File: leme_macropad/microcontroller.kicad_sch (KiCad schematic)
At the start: 23 parts, among them U1 W25Q128JVS, U2 RP2040, Y1 ABM8-272-T3

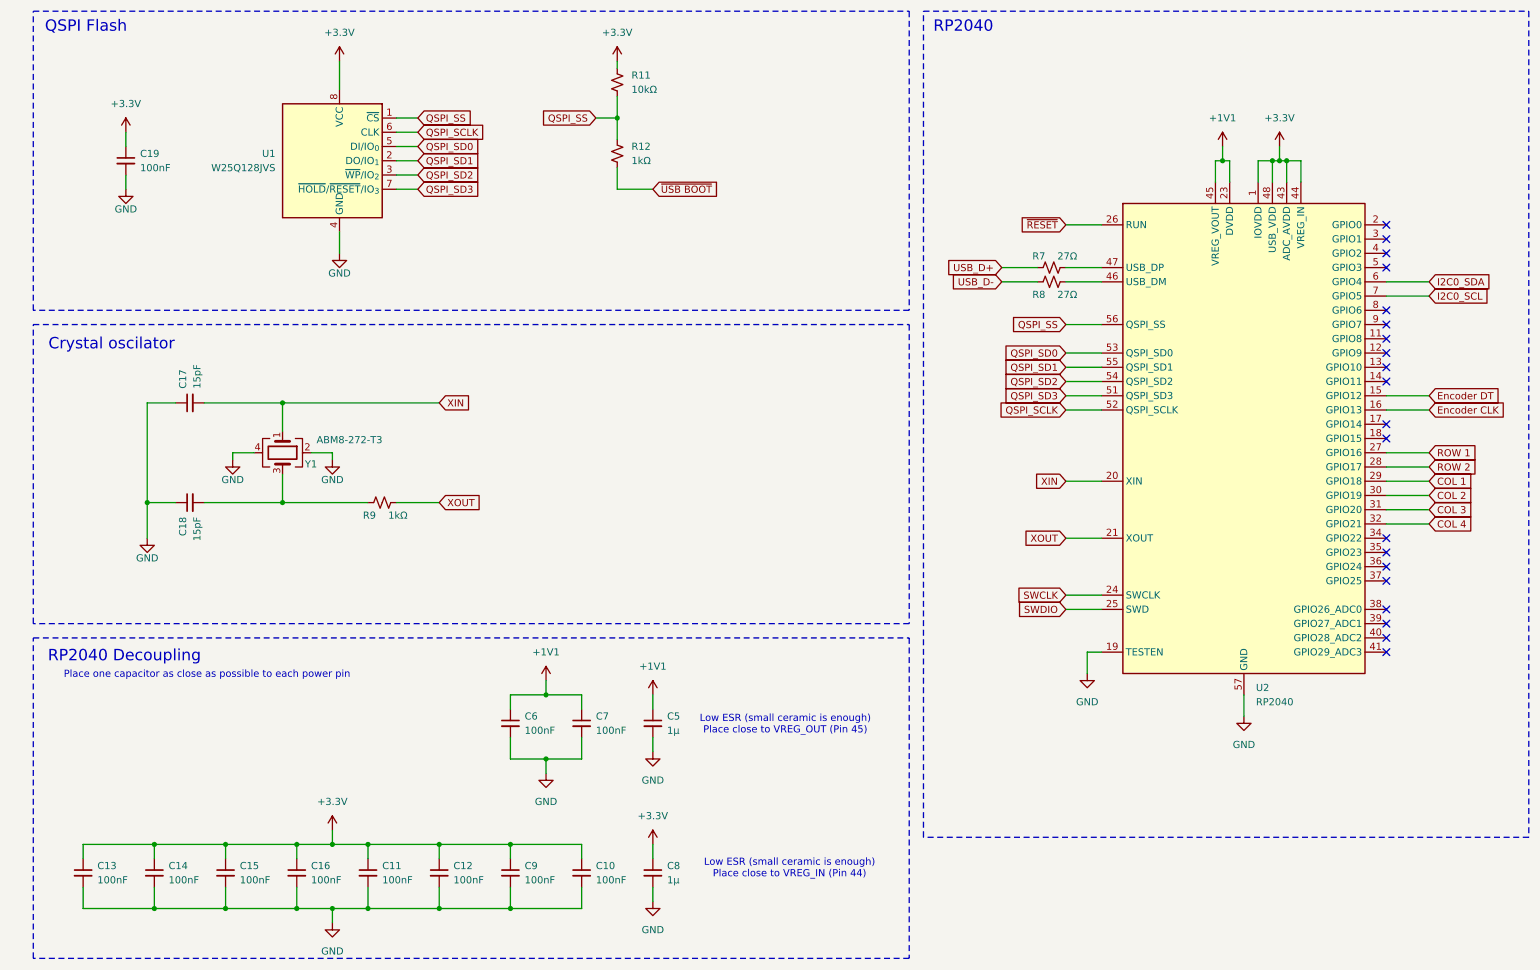
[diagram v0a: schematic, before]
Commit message: Annotates schematics again
Everything changed a lot, so it makes sense to reorder the components.
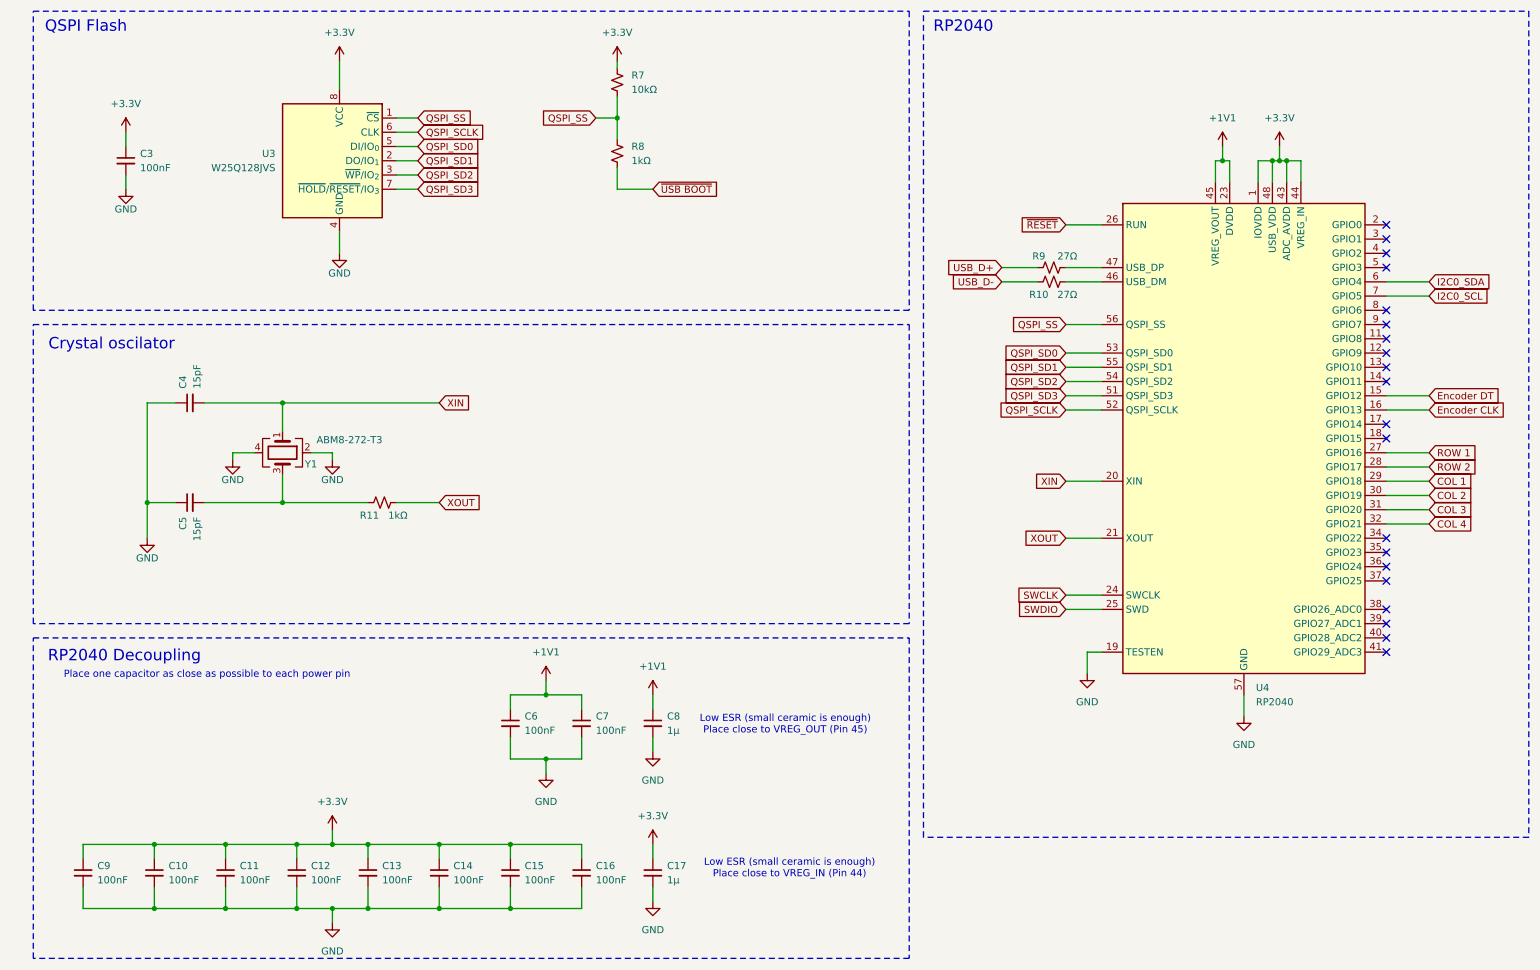
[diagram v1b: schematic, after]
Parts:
- renumbered C14 to C10, C15 to C11, C16 to C12, C11 to C13, C12 to C14, C9 to C15, C10 to C16, C8 to C17, C19 to C3, C17 to C4, C18 to C5, C5 to C8, C13 to C9, R8 to R10, R9 to R11, R11 to R7, R12 to R8, R7 to R9, U1 to U3, U2 to U4

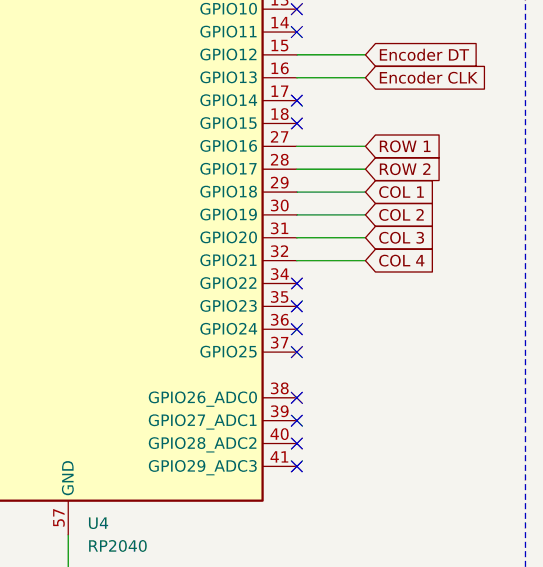
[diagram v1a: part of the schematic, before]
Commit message: Adds RGB LED matrix
There's only one per switch for now.
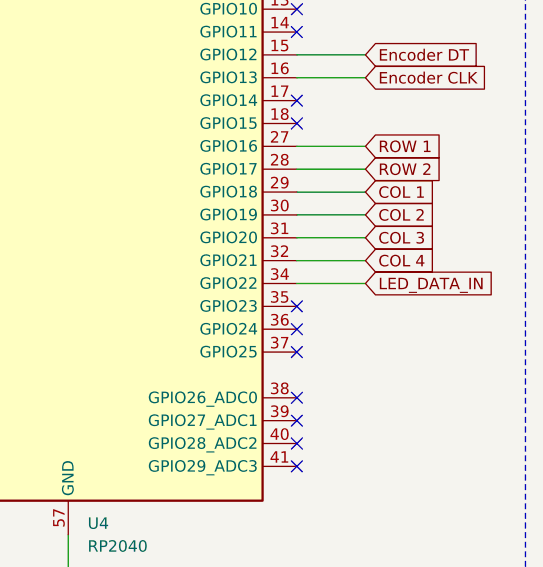
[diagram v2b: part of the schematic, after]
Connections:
- net LED_DATA_IN: now reaches U4.34 (GPIO22)
- no-connect marks 20 -> 19
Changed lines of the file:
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@@
-	)
-	(no_connect
-		(at 256.54 109.22)
 	)
 	(no_connect
@@
 	(wire
 		(pts
+			(xy 256.54 109.22) (xy 264.16 109.22)
+		)
+		(stroke
+			(width 0)
+			(type default)
+		)
+	)
+	(wire
+		(pts
 			(xy 59.69 85.09) (xy 45.72 85.09)
 		)
@@
 			(effects
 				(font
+					(size 1.27 1.27)
+				)
+				(justify left)
+				(hide yes)
+			)
+		)
+	)
+	(global_label "LED_DATA_IN"
+		(shape input)
+		(at 264.16 109.22 0)
+		(fields_autoplaced yes)
+		(effects
+			(font
+				(size 1.27 1.27)
+			)
+			(justify left)
+		)
+		(property "Intersheetrefs" "${INTERSHEET_REFS}"
+			(at 278.8776 109.22 0)
+			(effects
+				(font

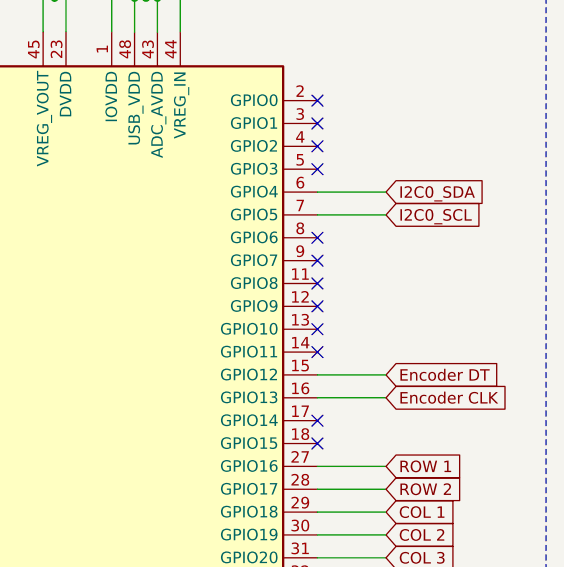
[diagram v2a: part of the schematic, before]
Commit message: Adds testpoints to some free GPIOs
It doesn't hurt to have them broken out if we need it.
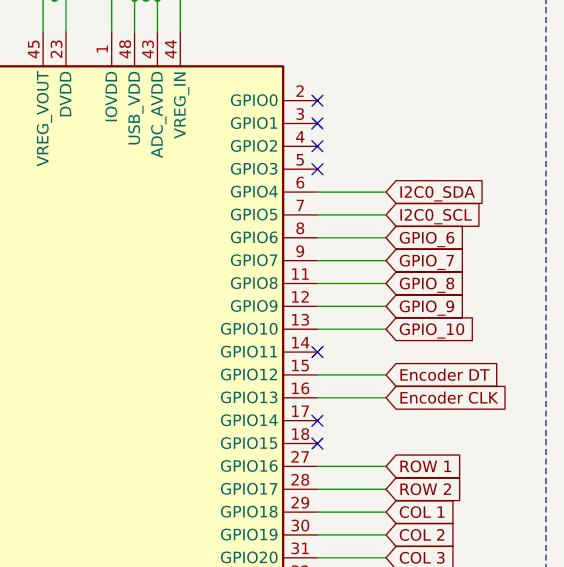
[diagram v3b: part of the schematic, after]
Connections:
- net GPIO_8: now reaches U4.11 (GPIO8)
- net GPIO_9: now reaches U4.12 (GPIO9)
- net GPIO_10: now reaches U4.13 (GPIO10)
- net GPIO_6: now reaches U4.8 (GPIO6)
- net GPIO_7: now reaches U4.9 (GPIO7)
- no-connect marks 19 -> 14
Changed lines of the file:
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@@
-	)
-	(no_connect
-		(at 256.54 73.66)
 	)
 	(no_connect
@@
 	)
 	(no_connect
-		(at 256.54 71.12)
+		(at 256.54 81.28)
 	)
 	(no_connect
@@
 	)
 	(no_connect
-		(at 256.54 81.28)
-	)
-	(no_connect
 		(at 256.54 91.44)
 	)
@@
 	)
 	(no_connect
-		(at 256.54 68.58)
-	)
-	(no_connect
-		(at 256.54 78.74)
-	)
-	(no_connect
 		(at 256.54 55.88)
 	)
@@
 		(at 256.54 60.96)
 	)
-	(no_connect
-		(at 256.54 76.2)
-	)
 	(wire
 		(pts
@@
 	(wire
 		(pts
+			(xy 256.54 73.66) (xy 264.16 73.66)
+		)
+		(stroke
+			(width 0)
+			(type default)
+		)
+	)
+	(wire
+		(pts
 			(xy 226.06 45.72) (xy 226.06 41.91)
 		)
@@
 	(wire
 		(pts
+			(xy 256.54 71.12) (xy 264.16 71.12)
+		)
+		(stroke
+			(width 0)
+			(type default)
+		)
+	)
+	(wire
+		(pts
 			(xy 199.39 63.5) (xy 205.74 63.5)
 		)
@@
 	(wire
 		(pts
+			(xy 256.54 68.58) (xy 264.16 68.58)
+		)
+		(stroke
+			(width 0)
+			(type default)
+		)
+	)
+	(wire
+		(pts
 			(xy 199.39 109.22) (xy 205.74 109.22)
 		)
@@
 	(wire
 		(pts
+			(xy 256.54 76.2) (xy 264.16 76.2)
+		)
+		(stroke
+			(width 0)
+			(type default)
+		)
+	)
+	(wire
+		(pts
 			(xy 106.68 137.16) (xy 113.03 137.16)
 		)
@@
 	(wire
 		(pts
+			(xy 256.54 78.74) (xy 264.16 78.74)
+		)
+		(stroke
+			(width 0)
+			(type default)
+		)
+	)
+	(wire
+		(pts
 			(xy 24.13 171.45) (xy 24.13 175.26)
 		)
@@
 		)
 	)
+	(global_label "GPIO_7"
+		(shape input)
+		(at 264.16 71.12 0)
+		(fields_autoplaced yes)
+		(effects
+			(font
+				(size 1.27 1.27)
+			)
+			(justify left)
+		)
+		(property "Intersheetrefs" "${INTERSHEET_REFS}"
+			(at 273.7976 71.12 0)
+			(effects
+				(font
+					(size 1.27 1.27)
+				)
+				(justify left)
+				(hide yes)
+			)
+		)
+	)
 	(global_label "COL 4"
 		(shape input)
@@
 		)
 	)
+	(global_label "GPIO_8"
+		(shape input)
+		(at 264.16 73.66 0)
+		(fields_autoplaced yes)
+		(effects
+			(font
+				(size 1.27 1.27)
+			)
+			(justify left)
+		)
+		(property "Intersheetrefs" "${INTERSHEET_REFS}"
+			(at 273.7976 73.66 0)
+			(effects
+				(font
+					(size 1.27 1.27)
+				)
+				(justify left)
+				(hide yes)
+			)
+		)
+	)
 	(global_label "ROW 2"
 		(shape input)
@@
 		)
 	)
+	(global_label "GPIO_10"
+		(shape input)
+		(at 264.16 78.74 0)
+		(fields_autoplaced yes)
+		(effects
+			(font
+				(size 1.27 1.27)
+			)
+			(justify left)
+		)
+		(property "Intersheetrefs" "${INTERSHEET_REFS}"
+			(at 275.0071 78.74 0)
+			(effects
+				(font
+					(size 1.27 1.27)
+				)
+				(justify left)
+				(hide yes)
+			)
+		)
+	)
 	(global_label "XIN"
 		(shape input)
@@
 		)
 	)
+	(global_label "GPIO_9"
+		(shape input)
+		(at 264.16 76.2 0)
+		(fields_autoplaced yes)
+		(effects
+			(font
+				(size 1.27 1.27)
+			)
+			(justify left)
+		)
+		(property "Intersheetrefs" "${INTERSHEET_REFS}"
+			(at 273.7976 76.2 0)
+			(effects
+				(font
+					(size 1.27 1.27)
+				)
+				(justify left)
+				(hide yes)
+			)
+		)
+	)
 	(global_label "I2C0_SDA"
 		(shape input)
@@
 				(hide yes)
 			)
+		)
+	)
+	(global_label "GPIO_6"
+		(shape input)
+		(at 264.16 68.58 0)
+		(fields_autoplaced yes)
+		(effects
+			(font
+				(size 1.27 1.27)
+			)
+			(justify left)
+		)
+		(property "Intersheetrefs" "${INTERSHEET_REFS}"
+			(at 273.7976 68.58 0)
+			(effects
+				(font
+					(size 1.27 1.27)
+				)
+				(justify left)
+				(hide yes)
+			)

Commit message: Re-annotates schematics
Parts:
- renumbered C13 to C10, C14 to C11, C6 to C12, C15 to C13, C7 to C14, C16 to C15, C8 to C16, C9 to C3, C3 to C4, C10 to C5, C4 to C6, C5 to C7, C11 to C8, C12 to C9, R11 to R3, R7 to R4, R8 to R5, R9 to R6, R10 to R7

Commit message: Assigns footprints to all components in schematics
Passives are 0603, but if the layout gets too dificult (specially around
the RP2040) we might want to decrease the size.

The mechanical switches are set as hotswap sockets for Kailh v1/v2, but
after routing everything we might want to do a version for MX switches.
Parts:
- C10, C11, C12, C13, C14, C15, C16, C17, C3, C4, C5, C6, C7, C8, C9: footprint (none) -> Capacitor_SMD:C_0603_1608Metric_Pad1.08x0.95mm_HandSolder
- R3, R4, R5, R6, R7: footprint (none) -> Resistor_SMD:R_0603_1608Metric_Pad0.98x0.95mm_HandSolder
- Y1: footprint (none) -> Crystal:Crystal_SMD_3225-4Pin_3.2x2.5mm
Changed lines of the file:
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@@
 			)
 		)
-		(property "Footprint" ""
+		(property "Footprint" "Capacitor_SMD:C_0603_1608Metric_Pad1.08x0.95mm_HandSolder"
 			(at 31.75 41.91 0)
 			(effects
@@
 			)
 		)
-		(property "Footprint" ""
+		(property "Footprint" "Resistor_SMD:R_0603_1608Metric_Pad0.98x0.95mm_HandSolder"
 			(at 119.38 40.64 0)
 			(effects
@@
 			)
 		)
-		(property "Footprint" ""
+		(property "Footprint" "Resistor_SMD:R_0603_1608Metric_Pad0.98x0.95mm_HandSolder"
 			(at 196.85 60.96 0)
 			(effects
@@
 			)
 		)
-		(property "Footprint" ""
+		(property "Footprint" "Capacitor_SMD:C_0603_1608Metric_Pad1.08x0.95mm_HandSolder"
 			(at 43.18 85.09 0)
 			(effects
@@
 			)
 		)
-		(property "Footprint" ""
+		(property "Footprint" "Capacitor_SMD:C_0603_1608Metric_Pad1.08x0.95mm_HandSolder"
 			(at 100.33 142.24 0)
 			(effects
@@
 			)
 		)
-		(property "Footprint" ""
+		(property "Footprint" "Capacitor_SMD:C_0603_1608Metric_Pad1.08x0.95mm_HandSolder"
 			(at 49.53 168.91 0)
 			(effects
@@
 			)
 		)
-		(property "Footprint" ""
+		(property "Footprint" "Resistor_SMD:R_0603_1608Metric_Pad0.98x0.95mm_HandSolder"
 			(at 196.85 63.5 0)
 			(effects
@@
 			)
 		)
-		(property "Footprint" ""
+		(property "Footprint" "Capacitor_SMD:C_0603_1608Metric_Pad1.08x0.95mm_HandSolder"
 			(at 62.23 168.91 0)
 			(effects
@@
 			)
 		)
-		(property "Footprint" ""
+		(property "Footprint" "Capacitor_SMD:C_0603_1608Metric_Pad1.08x0.95mm_HandSolder"
 			(at 43.18 102.87 0)
 			(effects
@@
 			)
 		)
-		(property "Footprint" ""
+		(property "Footprint" "Capacitor_SMD:C_0603_1608Metric_Pad1.08x0.95mm_HandSolder"
 			(at 125.73 142.24 0)
 			(effects
@@
 			)
 		)
-		(property "Footprint" ""
+		(property "Footprint" "Capacitor_SMD:C_0603_1608Metric_Pad1.08x0.95mm_HandSolder"
 			(at 113.03 168.91 0)
 			(effects
@@
 			)
 		)
-		(property "Footprint" ""
+		(property "Footprint" "Capacitor_SMD:C_0603_1608Metric_Pad1.08x0.95mm_HandSolder"
 			(at 24.13 168.91 0)
 			(effects
@@
 			)
 		)
-		(property "Footprint" ""
+		(property "Footprint" "Capacitor_SMD:C_0603_1608Metric_Pad1.08x0.95mm_HandSolder"
 			(at 125.73 168.91 0)
 			(effects
@@
 			)
 		)
-		(property "Footprint" ""
+		(property "Footprint" "Resistor_SMD:R_0603_1608Metric_Pad0.98x0.95mm_HandSolder"
 			(at 119.38 27.94 0)
 			(effects
@@
 			)
 		)
-		(property "Footprint" ""
+		(property "Footprint" "Resistor_SMD:R_0603_1608Metric_Pad0.98x0.95mm_HandSolder"
 			(at 77.47 102.87 0)
 			(effects
@@
 			)
 		)
-		(property "Footprint" ""
+		(property "Footprint" "Capacitor_SMD:C_0603_1608Metric_Pad1.08x0.95mm_HandSolder"
 			(at 87.63 168.91 0)
 			(effects
@@
 			)
 		)
-		(property "Footprint" ""
+		(property "Footprint" "Crystal:Crystal_SMD_3225-4Pin_3.2x2.5mm"
 			(at 59.69 93.98 0)
 			(effects
@@
 			)
 		)
-		(property "Footprint" ""
+		(property "Footprint" "Capacitor_SMD:C_0603_1608Metric_Pad1.08x0.95mm_HandSolder"
 			(at 74.93 168.91 0)
 			(effects
@@
 			)
 		)
-		(property "Footprint" ""
+		(property "Footprint" "Capacitor_SMD:C_0603_1608Metric_Pad1.08x0.95mm_HandSolder"
 			(at 113.03 142.24 0)
 			(effects
@@
 			)
 		)
-		(property "Footprint" ""
+		(property "Footprint" "Capacitor_SMD:C_0603_1608Metric_Pad1.08x0.95mm_HandSolder"
 			(at 100.33 168.91 0)
 			(effects
@@
 			)
 		)
-		(property "Footprint" ""
+		(property "Footprint" "Capacitor_SMD:C_0603_1608Metric_Pad1.08x0.95mm_HandSolder"
 			(at 36.83 168.91 0)
 			(effects

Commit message: Changes resistors and capacitors to 0402
This should make it much easier to route things and to comply with the
signal integrity needs of some parts of the circuit.
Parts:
- C10, C11, C12, C13, C14, C15, C16, C17, C3, C4, C5, C6, C7, C8, C9: footprint Capacitor_SMD:C_0603_1608Metric_Pad1.08x0.95mm_HandSolder -> Capacitor_SMD:C_0402_1005Metric_Pad0.74x0.62mm_HandSolder
- R3, R4, R5, R6, R7: footprint Resistor_SMD:R_0603_1608Metric_Pad0.98x0.95mm_HandSolder -> Resistor_SMD:R_0402_1005Metric_Pad0.72x0.64mm_HandSolder
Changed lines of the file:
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@@
 			)
 		)
-		(property "Footprint" "Capacitor_SMD:C_0603_1608Metric_Pad1.08x0.95mm_HandSolder"
+		(property "Footprint" "Capacitor_SMD:C_0402_1005Metric_Pad0.74x0.62mm_HandSolder"
 			(at 31.75 41.91 0)
 			(effects
@@
 			)
 		)
-		(property "Footprint" "Resistor_SMD:R_0603_1608Metric_Pad0.98x0.95mm_HandSolder"
+		(property "Footprint" "Resistor_SMD:R_0402_1005Metric_Pad0.72x0.64mm_HandSolder"
 			(at 119.38 40.64 0)
 			(effects
@@
 			)
 		)
-		(property "Footprint" "Resistor_SMD:R_0603_1608Metric_Pad0.98x0.95mm_HandSolder"
+		(property "Footprint" "Resistor_SMD:R_0402_1005Metric_Pad0.72x0.64mm_HandSolder"
 			(at 196.85 60.96 0)
 			(effects
@@
 			)
 		)
-		(property "Footprint" "Capacitor_SMD:C_0603_1608Metric_Pad1.08x0.95mm_HandSolder"
+		(property "Footprint" "Capacitor_SMD:C_0402_1005Metric_Pad0.74x0.62mm_HandSolder"
 			(at 43.18 85.09 0)
 			(effects
@@
 			)
 		)
-		(property "Footprint" "Capacitor_SMD:C_0603_1608Metric_Pad1.08x0.95mm_HandSolder"
+		(property "Footprint" "Capacitor_SMD:C_0402_1005Metric_Pad0.74x0.62mm_HandSolder"
 			(at 100.33 142.24 0)
 			(effects
@@
 			)
 		)
-		(property "Footprint" "Capacitor_SMD:C_0603_1608Metric_Pad1.08x0.95mm_HandSolder"
+		(property "Footprint" "Capacitor_SMD:C_0402_1005Metric_Pad0.74x0.62mm_HandSolder"
 			(at 49.53 168.91 0)
 			(effects
@@
 			)
 		)
-		(property "Footprint" "Resistor_SMD:R_0603_1608Metric_Pad0.98x0.95mm_HandSolder"
+		(property "Footprint" "Resistor_SMD:R_0402_1005Metric_Pad0.72x0.64mm_HandSolder"
 			(at 196.85 63.5 0)
 			(effects
@@
 			)
 		)
-		(property "Footprint" "Capacitor_SMD:C_0603_1608Metric_Pad1.08x0.95mm_HandSolder"
+		(property "Footprint" "Capacitor_SMD:C_0402_1005Metric_Pad0.74x0.62mm_HandSolder"
 			(at 62.23 168.91 0)
 			(effects
@@
 			)
 		)
-		(property "Footprint" "Capacitor_SMD:C_0603_1608Metric_Pad1.08x0.95mm_HandSolder"
+		(property "Footprint" "Capacitor_SMD:C_0402_1005Metric_Pad0.74x0.62mm_HandSolder"
 			(at 43.18 102.87 0)
 			(effects
@@
 			)
 		)
-		(property "Footprint" "Capacitor_SMD:C_0603_1608Metric_Pad1.08x0.95mm_HandSolder"
+		(property "Footprint" "Capacitor_SMD:C_0402_1005Metric_Pad0.74x0.62mm_HandSolder"
 			(at 125.73 142.24 0)
 			(effects
@@
 			)
 		)
-		(property "Footprint" "Capacitor_SMD:C_0603_1608Metric_Pad1.08x0.95mm_HandSolder"
+		(property "Footprint" "Capacitor_SMD:C_0402_1005Metric_Pad0.74x0.62mm_HandSolder"
 			(at 113.03 168.91 0)
 			(effects
@@
 			)
 		)
-		(property "Footprint" "Capacitor_SMD:C_0603_1608Metric_Pad1.08x0.95mm_HandSolder"
+		(property "Footprint" "Capacitor_SMD:C_0402_1005Metric_Pad0.74x0.62mm_HandSolder"
 			(at 24.13 168.91 0)
 			(effects
@@
 			)
 		)
-		(property "Footprint" "Capacitor_SMD:C_0603_1608Metric_Pad1.08x0.95mm_HandSolder"
+		(property "Footprint" "Capacitor_SMD:C_0402_1005Metric_Pad0.74x0.62mm_HandSolder"
 			(at 125.73 168.91 0)
 			(effects
@@
 			)
 		)
-		(property "Footprint" "Resistor_SMD:R_0603_1608Metric_Pad0.98x0.95mm_HandSolder"
+		(property "Footprint" "Resistor_SMD:R_0402_1005Metric_Pad0.72x0.64mm_HandSolder"
 			(at 119.38 27.94 0)
 			(effects
@@
 			)
 		)
-		(property "Footprint" "Resistor_SMD:R_0603_1608Metric_Pad0.98x0.95mm_HandSolder"
+		(property "Footprint" "Resistor_SMD:R_0402_1005Metric_Pad0.72x0.64mm_HandSolder"
 			(at 77.47 102.87 0)
 			(effects
@@
 			)
 		)
-		(property "Footprint" "Capacitor_SMD:C_0603_1608Metric_Pad1.08x0.95mm_HandSolder"
+		(property "Footprint" "Capacitor_SMD:C_0402_1005Metric_Pad0.74x0.62mm_HandSolder"
 			(at 87.63 168.91 0)
 			(effects
@@
 			)
 		)
-		(property "Footprint" "Capacitor_SMD:C_0603_1608Metric_Pad1.08x0.95mm_HandSolder"
+		(property "Footprint" "Capacitor_SMD:C_0402_1005Metric_Pad0.74x0.62mm_HandSolder"
 			(at 74.93 168.91 0)
 			(effects
@@
 			)
 		)
-		(property "Footprint" "Capacitor_SMD:C_0603_1608Metric_Pad1.08x0.95mm_HandSolder"
+		(property "Footprint" "Capacitor_SMD:C_0402_1005Metric_Pad0.74x0.62mm_HandSolder"
 			(at 113.03 142.24 0)
 			(effects
@@
 			)
 		)
-		(property "Footprint" "Capacitor_SMD:C_0603_1608Metric_Pad1.08x0.95mm_HandSolder"
+		(property "Footprint" "Capacitor_SMD:C_0402_1005Metric_Pad0.74x0.62mm_HandSolder"
 			(at 100.33 168.91 0)
 			(effects
@@
 			)
 		)
-		(property "Footprint" "Capacitor_SMD:C_0603_1608Metric_Pad1.08x0.95mm_HandSolder"
+		(property "Footprint" "Capacitor_SMD:C_0402_1005Metric_Pad0.74x0.62mm_HandSolder"
 			(at 36.83 168.91 0)
 			(effects
